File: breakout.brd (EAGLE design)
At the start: 25.4 x 32.4 mm, 22 parts, among them IC2 REG1117, U4 FT232R

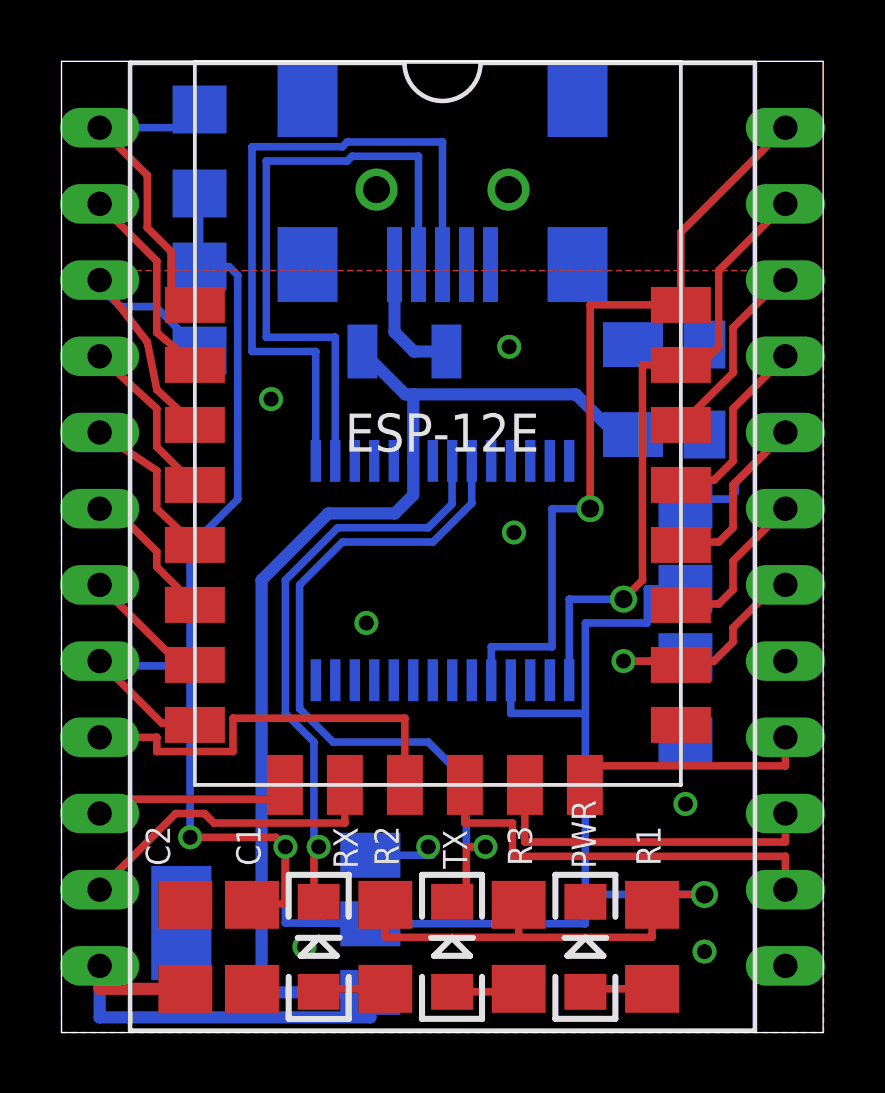
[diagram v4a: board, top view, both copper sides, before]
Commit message: CH340G
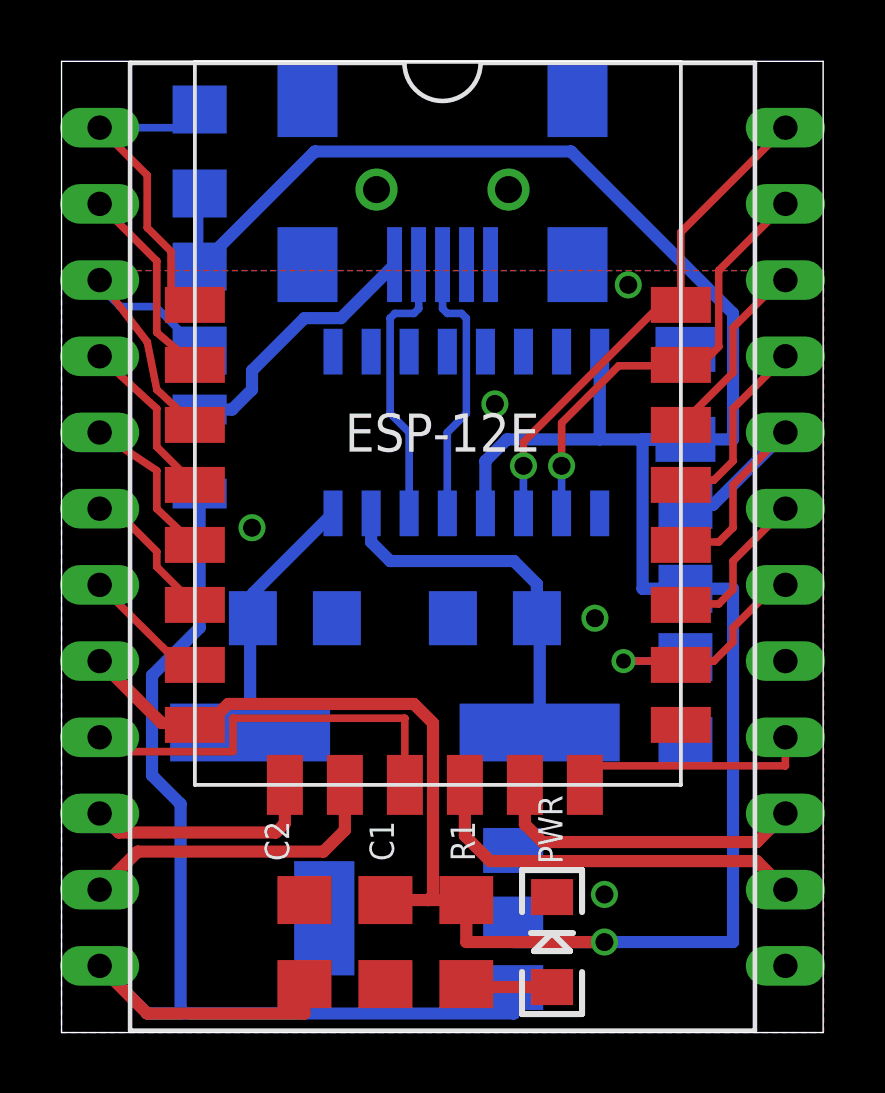
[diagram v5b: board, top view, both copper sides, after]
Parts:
- removed R2, R3: 330, SparkFun-Passives:1206
- removed RX: RED, SparkFun-LED:LED-1206
- removed TX: GREEN, SparkFun-LED:LED-1206
- removed U4: FT232R, SparkFun:SSOP28DB
- added C5: 22pf, SparkFun-Capacitors:1206
- added U$1: CH340G, CH340G-USB-SERIAL:SOIC16
- added Y1: 12mhz, SparkFun-FreqCtrl:HC49UP
- C4: value 10uF -> 22pf; device rcl:SMC_A -> SparkFun-Capacitors:1206
- moved C4 10.3 mm to (14.4, 13.8), turned to 0 degrees
- moved F1 7.60 mm to (4.60, 19.4), turned to 270 degrees
- moved R1 6.19 mm to (13.5, 3.02)
- moved IC2 4.77 mm to (11.9, 3.81)
- moved C1 4.45 mm to (10.8, 3.02)
- moved C2 3.97 mm to (8.10, 3.02)
- moved C3 1.75 mm to (20.8, 21.3)
- moved LOGO1 1.21 mm to (20.6, 30.0)
- moved PWR 1.12 mm to (16.4, 3.02)
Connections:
- removed net N$2: R2.1, RX.A
- removed net N$3: R3.1, TX.A
- removed net PWREN: U4.14
- removed net RXLED: RX.C, U4.22
- removed net SLEEP: U4.12
- removed net TXDEN: U4.13
- removed net TXLED: TX.C, U4.23
- new net N$12: U$1.9
- new net N$13: U$1.10
- new net N$14: U$1.11
- new net N$15: U$1.12
- new net N$16: U$1.13
- new net N$17: U$1.14
- new net N$18: U$1.15
- new net OSCI: C4.1, U$1.7, Y1.1
- new net OSCO: C5.1, U$1.8, Y1.2
- net 3.3V: now also C3.1, U$1.16, U$1.4; no longer R2.2, R3.2, U4.4
- net 5V: no longer C3.1, C4.+, U4.20
- net GND: now also C4.2, C5.2, U$1.1; no longer C4.-, U4.18, U4.21, U4.25, U4.26, U4.7
- net RX: now also U$1.2; no longer U4.1
- net TX: now also U$1.3; no longer U4.5
- net USB_D+: now also U$1.5; no longer U4.15
- net USB_D-: now also U$1.6; no longer U4.16
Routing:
- net TXLED: track 24.8 -> 0.00 mm, vias 1 -> 0
- net RXLED: track 19.6 -> 0.00 mm, vias 1 -> 0
- net USB_D+: track 23.1 -> 9.16 mm
- net 3.3V: track 86.0 -> 99.4 mm, vias 3 -> 1
- net 5V: track 54.7 -> 42.3 mm
- net OSCI: track 0.00 -> 12.1 mm
- net USB_D-: track 21.0 -> 9.32 mm
- net TX: track 26.2 -> 16.9 mm
- net OSCO: track 0.00 -> 8.45 mm
- net RX: track 21.1 -> 15.3 mm
- net USB_VIN: track 4.25 -> 8.87 mm
- net GND: track 2.51 -> 0.00 mm, vias 8 -> 5
- net N$3: track 2.32 -> 0.00 mm
- net N$2: track 2.32 -> 0.00 mm
- net SCLK: track 14.2 -> 13.1 mm
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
